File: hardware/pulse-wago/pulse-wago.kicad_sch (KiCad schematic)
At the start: 44 parts, among them J101 Cortex, SW101 SKSG, SW102 SKSG, U101 ATSAMD51J, U102 TPS78433QWDRBRQ1, Y101 32k768

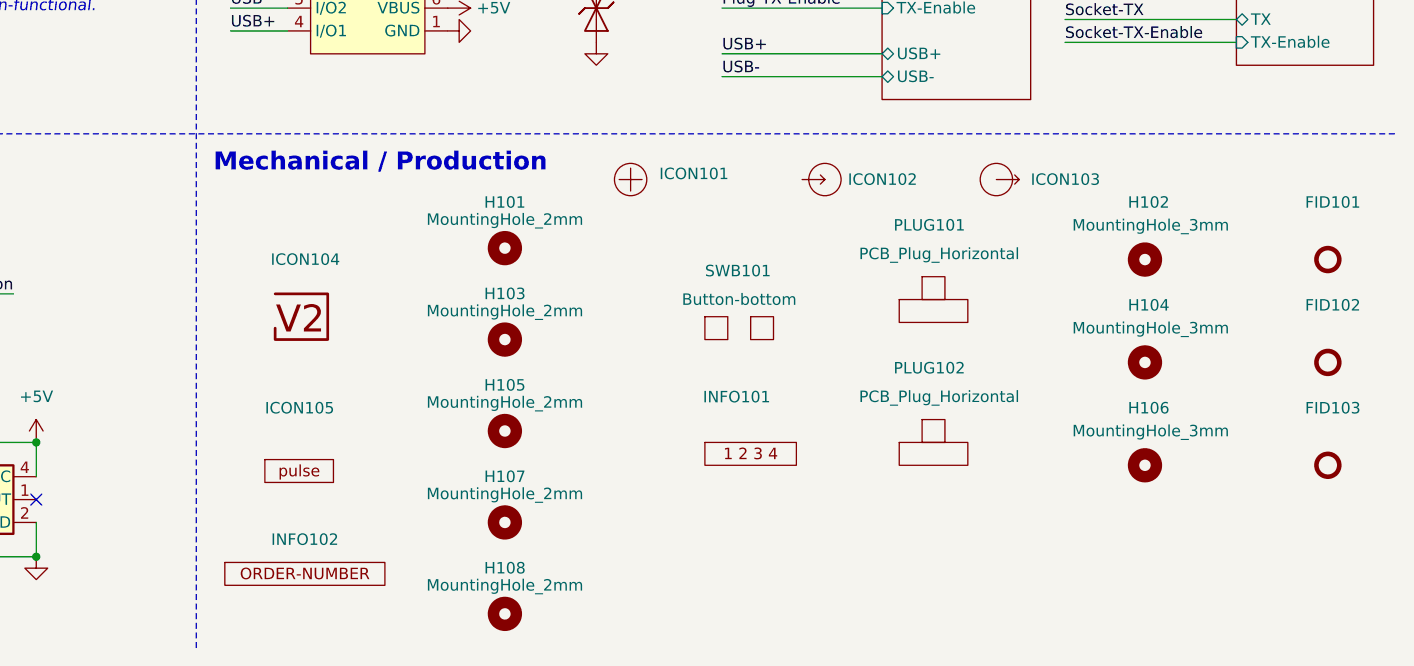
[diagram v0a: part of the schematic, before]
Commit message: Replace Order_Number
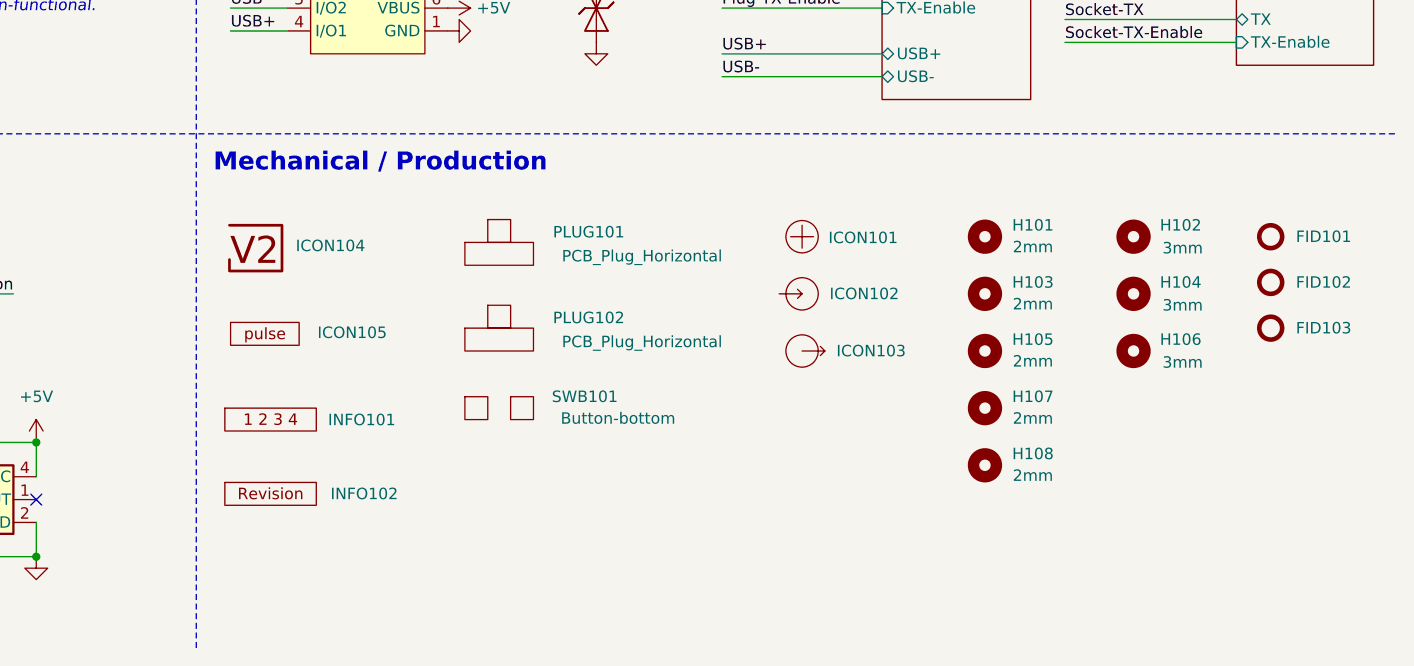
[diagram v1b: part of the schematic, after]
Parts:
- H101, H103, H105, H107, H108: value MountingHole_2mm -> 2mm
- H102, H104, H106: value MountingHole_3mm -> 3mm
- INFO102: value Order_Number -> (none); footprint V2_Production:Order_Number -> V2_Production:Revision; symbol V2_Production:Order_Number -> V2_Production:Revision
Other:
- moved on the sheet: FID101, FID102, FID103, H101, H102, H103, H104, H105, H106, H107, H108, ICON101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

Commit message: Update Library
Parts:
- C101: symbol V2_Device:C_0603_10u -> V2_Capacitor:0603_10u
- C102, C103, C104, C105, C106: symbol V2_Device:C_0603_0u1 -> V2_Capacitor:0603_0u1
- C107, C108: symbol V2_Device:C_0603_18p -> V2_Capacitor:0603_18p
- C109, C110: symbol V2_Device:C_0805_10u -> V2_Capacitor:0805_10u
- D101: symbol V2_Device:LED_0603_Orange -> V2_LED:0603_Orange
- R101: symbol V2_Device:R_0603_330R -> V2_Resistor:0603_330R
- R102: symbol V2_Device:R_0603_100k -> V2_Resistor:0603_100k
- Y101: symbol V2_Device:Crystal_3.2x1.5_32k768 -> V2_Crystal:3.2x1.5_32k768
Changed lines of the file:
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@@
 		(on_board yes)
 		(dnp no)
-		(property "Reference" "#PWR0116"
+		(property "Reference" "#PWR116"
 			(at 175.26 125.73 0)
 			(effects
@@
 			(project "pulse"
 				(path "/6c8448b4-b04d-47e1-934e-e40cbe27a7be"
-					(reference "#PWR0116")
+					(reference "#PWR116")
 					(unit 1)
 				)
@@
 		(on_board yes)
 		(dnp no)
-		(property "Reference" "#PWR0114"
+		(property "Reference" "#PWR114"
 			(at 195.58 125.73 0)
 			(effects
@@
 			(project "pulse"
 				(path "/6c8448b4-b04d-47e1-934e-e40cbe27a7be"
-					(reference "#PWR0114")
+					(reference "#PWR114")
 					(unit 1)
 				)
@@
 	)
 	(symbol
-		(lib_id "V2_Device:C_0603_0u1")
+		(lib_id "V2_Capacitor:0603_0u1")
 		(at 109.22 24.13 0)
 		(unit 1)
@@
 		(on_board yes)
 		(dnp no)
-		(property "Reference" "#PWR0127"
+		(property "Reference" "#PWR127"
 			(at 133.35 193.04 0)
 			(effects
@@
 			(project "pulse"
 				(path "/6c8448b4-b04d-47e1-934e-e40cbe27a7be"
-					(reference "#PWR0127")
+					(reference "#PWR127")
 					(unit 1)
 				)
@@
 		(on_board yes)
 		(dnp no)
-		(property "Reference" "#PWR0122"
+		(property "Reference" "#PWR122"
 			(at 58.42 170.18 0)
 			(effects
@@
 			(project "pulse"
 				(path "/6c8448b4-b04d-47e1-934e-e40cbe27a7be"
-					(reference "#PWR0122")
+					(reference "#PWR122")
 					(unit 1)
 				)
@@
 		(on_board yes)
 		(dnp no)
-		(property "Reference" "#PWR0124"
+		(property "Reference" "#PWR124"
 			(at 58.42 177.8 0)
 			(effects
@@
 			(project "pulse"
 				(path "/6c8448b4-b04d-47e1-934e-e40cbe27a7be"
-					(reference "#PWR0124")
+					(reference "#PWR124")
 					(unit 1)
 				)
@@
 		(on_board yes)
 		(dnp no)
-		(property "Reference" "#PWR0117"
+		(property "Reference" "#PWR117"
 			(at 67.31 133.35 0)
 			(effects
@@
 			(project "pulse"
 				(path "/6c8448b4-b04d-47e1-934e-e40cbe27a7be"
-					(reference "#PWR0117")
+					(reference "#PWR117")
 					(unit 1)
 				)
@@
 		(on_board yes)
 		(dnp no)
-		(property "Reference" "#PWR0107"
+		(property "Reference" "#PWR107"
 			(at 26.67 55.88 0)
 			(effects
@@
 			(project "pulse"
 				(path "/6c8448b4-b04d-47e1-934e-e40cbe27a7be"
-					(reference "#PWR0107")
+					(reference "#PWR107")
 					(unit 1)
 				)
@@
 	)
 	(symbol
-		(lib_id "V2_Device:LED_0603_Orange")
+		(lib_id "V2_LED:0603_Orange")
 		(at 125.73 86.36 0)
 		(mirror y)
@@
 		(on_board yes)
 		(dnp no)
-		(property "Reference" "#PWR0102"
+		(property "Reference" "#PWR102"
 			(at 57.15 33.02 0)
 			(effects
@@
 			(project "pulse"
 				(path "/6c8448b4-b04d-47e1-934e-e40cbe27a7be"
-					(reference "#PWR0102")
+					(reference "#PWR102")
 					(unit 1)
 				)
@@
 	)
 	(symbol
-		(lib_id "V2_Device:C_0805_10u")
+		(lib_id "V2_Capacitor:0805_10u")
 		(at 58.42 168.91 0)
 		(unit 1)
@@
 		(on_board yes)
 		(dnp no)
-		(property "Reference" "#PWR0101"
+		(property "Reference" "#PWR101"
 			(at 72.39 25.4 0)
 			(effects
@@
 			(project "pulse"
 				(path "/6c8448b4-b04d-47e1-934e-e40cbe27a7be"
-					(reference "#PWR0101")
+					(reference "#PWR101")
 					(unit 1)
 				)
@@
 		(on_board yes)
 		(dnp no)
-		(property "Reference" "#PWR0125"
+		(property "Reference" "#PWR125"
 			(at 133.35 177.8 0)
 			(effects
@@
 			(project "pulse"
 				(path "/6c8448b4-b04d-47e1-934e-e40cbe27a7be"
-					(reference "#PWR0125")
+					(reference "#PWR125")
 					(unit 1)
 				)
@@
 		(on_board yes)
 		(dnp no)
-		(property "Reference" "#PWR0113"
+		(property "Reference" "#PWR113"
 			(at 52.07 121.92 0)
 			(effects
@@
 			(project "pulse"
 				(path "/6c8448b4-b04d-47e1-934e-e40cbe27a7be"
-					(reference "#PWR0113")
+					(reference "#PWR113")
 					(unit 1)
 				)
@@
 	)
 	(symbol
-		(lib_id "V2_Device:C_0603_0u1")
+		(lib_id "V2_Capacitor:0603_0u1")
 		(at 119.38 24.13 0)
 		(unit 1)
@@
 		(on_board yes)
 		(dnp no)
-		(property "Reference" "#PWR0106"
+		(property "Reference" "#PWR106"
 			(at 21.59 55.88 0)
 			(effects
@@
 			(project "pulse"
 				(path "/6c8448b4-b04d-47e1-934e-e40cbe27a7be"
-					(reference "#PWR0106")
+					(reference "#PWR106")
 					(unit 1)
 				)
@@
 		(on_board yes)
 		(dnp no)
-		(property "Reference" "#PWR0111"
+		(property "Reference" "#PWR111"
 			(at 106.68 113.03 0)
 			(effects
@@
 			(project "pulse"
 				(path "/6c8448b4-b04d-47e1-934e-e40cbe27a7be"
-					(reference "#PWR0111")
+					(reference "#PWR111")
 					(unit 1)
 				)
@@
 		(on_board yes)
 		(dnp no)
-		(property "Reference" "#PWR0118"
+		(property "Reference" "#PWR118"
 			(at 185.42 128.27 0)
 			(effects
@@
 			(project "pulse"
 				(path "/6c8448b4-b04d-47e1-934e-e40cbe27a7be"
-					(reference "#PWR0118")
+					(reference "#PWR118")
 					(unit 1)
 				)
@@
 		(on_board yes)
 		(dnp no)
-		(property "Reference" "#PWR0121"
+		(property "Reference" "#PWR121"
 			(at 33.02 170.18 0)
 			(effects
@@
 			(project "pulse"
 				(path "/6c8448b4-b04d-47e1-934e-e40cbe27a7be"
-					(reference "#PWR0121")
+					(reference "#PWR121")
 					(unit 1)
 				)
@@
 		(on_board yes)
 		(dnp no)
-		(property "Reference" "#PWR0104"
+		(property "Reference" "#PWR104"
 			(at 57.15 48.26 0)
 			(effects
@@
 			(project "pulse"
 				(path "/6c8448b4-b04d-47e1-934e-e40cbe27a7be"
-					(reference "#PWR0104")
+					(reference "#PWR104")
 					(unit 1)
 				)
@@
 		(on_board yes)
 		(dnp no)
-		(property "Reference" "#PWR0103"
+		(property "Reference" "#PWR103"
 			(at 78.74 33.02 0)
 			(effects
@@
 			(project "pulse"
 				(path "/6c8448b4-b04d-47e1-934e-e40cbe27a7be"
-					(reference "#PWR0103")
+					(reference "#PWR103")
 					(unit 1)
 				)
@@
 		(on_board yes)
 		(dnp no)
-		(property "Reference" "#PWR0115"
+		(property "Reference" "#PWR115"
 			(at 260.35 121.92 0)
 			(effects
@@
 			(project "pulse"
 				(path "/6c8448b4-b04d-47e1-934e-e40cbe27a7be"
-					(reference "#PWR0115")
+					(reference "#PWR115")
 					(unit 1)
 				)
@@
 		(on_board yes)
 		(dnp no)
-		(property "Reference" "#PWR0120"
+		(property "Reference" "#PWR120"
 			(at 106.68 157.48 0)
 			(effects
@@
 			(project "pulse"
 				(path "/6c8448b4-b04d-47e1-934e-e40cbe27a7be"
-					(reference "#PWR0120")
+					(reference "#PWR120")
 					(unit 1)
 				)
@@
 		(on_board yes)
 		(dnp no)
-		(property "Reference" "#PWR0110"
+		(property "Reference" "#PWR110"
 			(at 116.84 102.87 0)
 			(effects
@@
 			(project "pulse"
 				(path "/6c8448b4-b04d-47e1-934e-e40cbe27a7be"
-					(reference "#PWR0110")
+					(reference "#PWR110")
 					(unit 1)
 				)
@@
 	)
 	(symbol
-		(lib_id "V2_Device:C_0805_10u")
+		(lib_id "V2_Capacitor:0805_10u")
 		(at 33.02 168.91 0)
 		(unit 1)
@@
 	)
 	(symbol
-		(lib_id "V2_Device:Crystal_3.2x1.5_32k768")
+		(lib_id "V2_Crystal:3.2x1.5_32k768")
 		(at 24.13 43.18 0)
 		(unit 1)
@@
 	)
 	(symbol
-		(lib_id "V2_Device:C_0603_18p")
+		(lib_id "V2_Capacitor:0603_18p")
 		(at 26.67 46.99 0)
 		(unit 1)
@@
 	)
 	(symbol
-		(lib_id "V2_Device:C_0603_10u")
+		(lib_id "V2_Capacitor:0603_10u")
 		(at 57.15 24.13 0)
 		(unit 1)
@@
 		(on_board yes)
 		(dnp no)
-		(property "Reference" "#PWR0123"
+		(property "Reference" "#PWR123"
 			(at 33.02 177.8 0)
 			(effects
@@
 			(project "pulse"
 				(path "/6c8448b4-b04d-47e1-934e-e40cbe27a7be"
-					(reference "#PWR0123")
+					(reference "#PWR123")
 					(unit 1)
 				)
@@
 	)
 	(symbol
-		(lib_id "V2_Device:C_0603_18p")
+		(lib_id "V2_Capacitor:0603_18p")
 		(at 21.59 46.99 0)
 		(unit 1)
@@
 		(on_board yes)
 		(dnp no)
-		(property "Reference" "#PWR0126"
+		(property "Reference" "#PWR126"
 			(at 45.72 182.88 0)
 			(effects
@@
 			(project "pulse"
 				(path "/6c8448b4-b04d-47e1-934e-e40cbe27a7be"
-					(reference "#PWR0126")
+					(reference "#PWR126")
 					(unit 1)
 				)
@@
 		(on_board yes)
 		(dnp no)
-		(property "Reference" "#PWR0109"
+		(property "Reference" "#PWR109"
 			(at 143.51 86.36 0)
 			(effects
@@
 			(project "pulse"
 				(path "/6c8448b4-b04d-47e1-934e-e40cbe27a7be"
-					(reference "#PWR0109")
+					(reference "#PWR109")
 					(unit 1)
 				)
@@
 	)
 	(symbol
-		(lib_id "V2_Device:R_0603_330R")
+		(lib_id "V2_Resistor:0603_330R")
 		(at 134.62 86.36 90)
 		(unit 1)
@@
 	)
 	(symbol
-		(lib_id "V2_Device:C_0603_0u1")
+		(lib_id "V2_Capacitor:0603_0u1")
 		(at 99.06 24.13 0)
 		(unit 1)
@@
 	)
 	(symbol
-		(lib_id "V2_Device:C_0603_0u1")
+		(lib_id "V2_Capacitor:0603_0u1")
 		(at 78.74 24.13 0)
 		(unit 1)
@@
 		(on_board yes)
 		(dnp no)
-		(property "Reference" "#PWR0105"
+		(property "Reference" "#PWR105"
 			(at 92.71 48.26 0)
 			(effects
@@
 			(project "pulse"
 				(path "/6c8448b4-b04d-47e1-934e-e40cbe27a7be"
-					(reference "#PWR0105")
+					(reference "#PWR105")
 					(unit 1)
 				)
@@
 		(on_board yes)
 		(dnp no)
-		(property "Reference" "#PWR0119"
+		(property "Reference" "#PWR119"
 			(at 195.58 135.89 0)
 			(effects
@@
 			(project "pulse"
 				(path "/6c8448b4-b04d-47e1-934e-e40cbe27a7be"
-					(reference "#PWR0119")
+					(reference "#PWR119")
 					(unit 1)
 				)
@@
 		(on_board yes)
 		(dnp no)
-		(property "Reference" "#PWR0108"
+		(property "Reference" "#PWR108"
 			(at 121.92 67.31 0)
 			(effects
@@
 			(project "pulse"
 				(path "/6c8448b4-b04d-47e1-934e-e40cbe27a7be"
-					(reference "#PWR0108")
+					(reference "#PWR108")
 					(unit 1)
 				)
@@
 		(on_board yes)
 		(dnp no)
-		(property "Reference" "#PWR0112"
+		(property "Reference" "#PWR112"
 			(at 220.98 118.11 0)
 			(effects
@@
 			(project "pulse"
 				(path "/6c8448b4-b04d-47e1-934e-e40cbe27a7be"
-					(reference "#PWR0112")
+					(reference "#PWR112")
 					(unit 1)
 				)
@@
 	)
 	(symbol
-		(lib_id "V2_Device:C_0603_0u1")
+		(lib_id "V2_Capacitor:0603_0u1")
 		(at 88.9 24.13 0)
 		(unit 1)
@@
 	)
 	(symbol
-		(lib_id "V2_Device:R_0603_100k")
+		(lib_id "V2_Resistor:0603_100k")
 		(at 50.8 121.92 90)
 		(unit 1)
